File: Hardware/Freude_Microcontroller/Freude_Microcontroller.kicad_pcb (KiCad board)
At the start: 4 copper layers, 20.6 x 22 mm, 22 parts, among them J2 Conn_01x05_Female, J3 Conn_01x06_Female, J4 Conn_01x06_Female, SW1 B3FS-1015P`, U2 STM32L432KBUx, Y1 Crystal_GND24

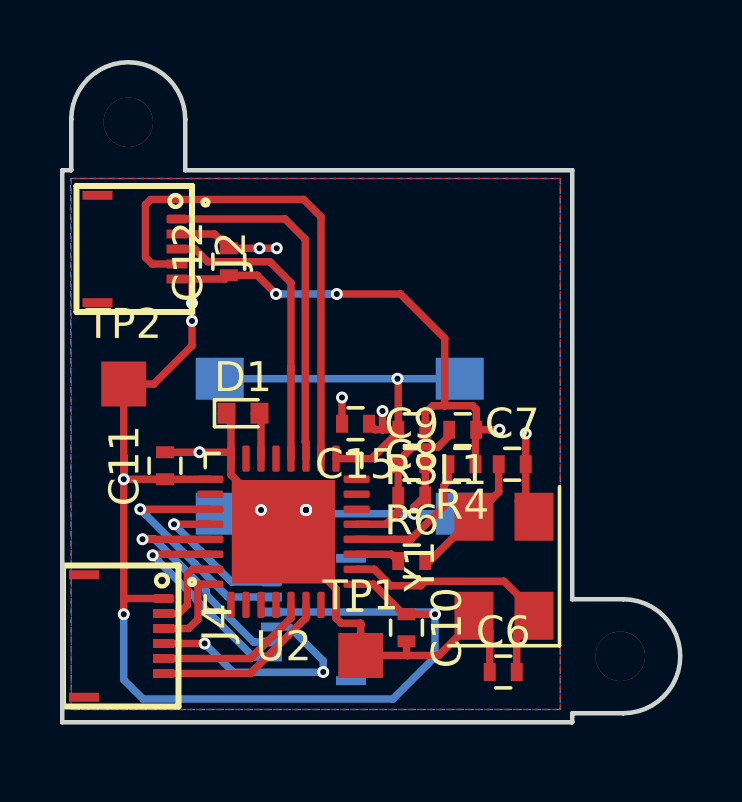
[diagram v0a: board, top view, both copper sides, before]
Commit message: made outline smaller to fit housing, subsequent rerouting
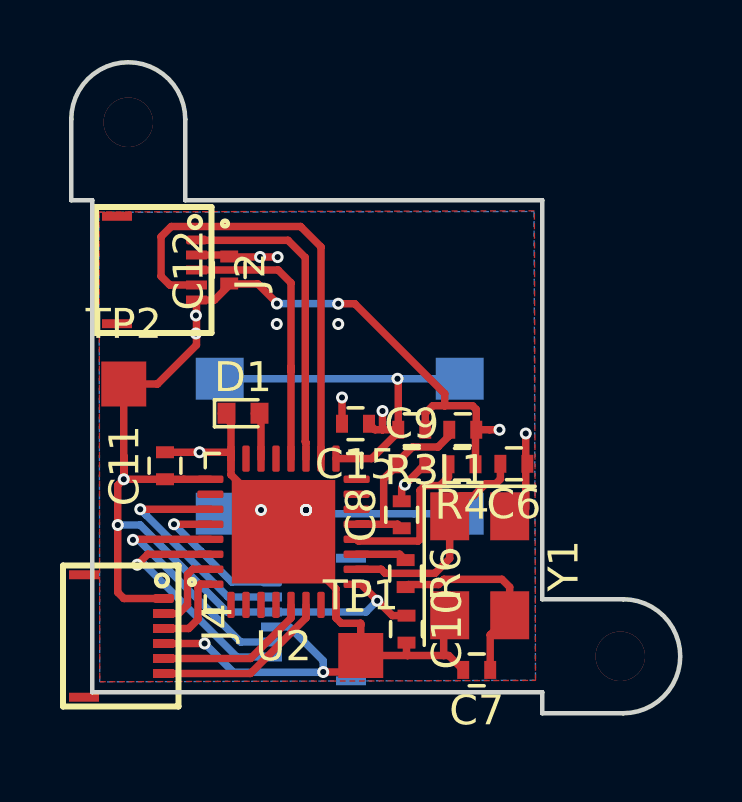
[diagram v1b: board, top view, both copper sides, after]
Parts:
- moved C7 6.96 mm to (205.3, 87.3), turned to 180 degrees
- moved C6 6.95 mm to (206.5, 80.4), turned to 180 degrees
- moved J2 0.96 mm to (195.9, 74.0)
- moved Y1 0.81 mm to (205.4, 83.8), turned to 270 degrees
- moved C8 0.72 mm to (202.8, 82.1), turned to 90 degrees
- moved R6 0.47 mm to (202.9, 84.1), turned to 270 degrees
- moved C12 0.28 mm to (197.0, 74.0)
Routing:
- net +1V8: track 58.4 -> 44.1 mm, vias 8 -> 10
- net GND: track 45.9 -> 44.1 mm
- net /DAC1_OUT2: track 17.1 -> 15.4 mm
- net Net-(C7-Pad1): track 5.14 -> 6.71 mm
- net /DAC2_OUT1: track 11.9 -> 10.5 mm
- net Net-(C6-Pad2): track 8.88 -> 7.55 mm
- net Net-(C8-Pad1): track 5.51 -> 6.68 mm
- net /AZO_UNK: track 7.32 -> 8.33 mm
- net /Switch_Out: track 10.3 -> 9.34 mm
- net /RDY_UC: track 8.06 -> 8.62 mm
- net Net-(R4-Pad2): track 4.83 -> 5.35 mm
- added copper zone on In1.Cu, net +1V8
- removed copper zone on In1.Cu, net +3V3
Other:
- board size 20.6 x 22 mm -> 20.3 x 21.7 mm

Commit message: silk layout, proto release candidate
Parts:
- renumbered REF** to Outline

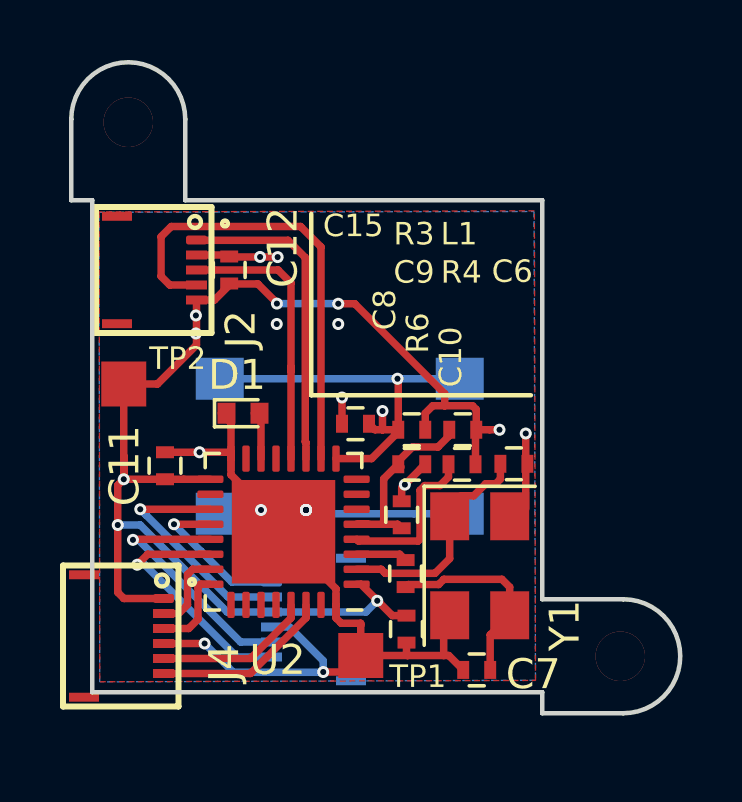
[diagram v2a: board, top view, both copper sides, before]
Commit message: change hole size to 0.45mm, decrease soldermask expansion
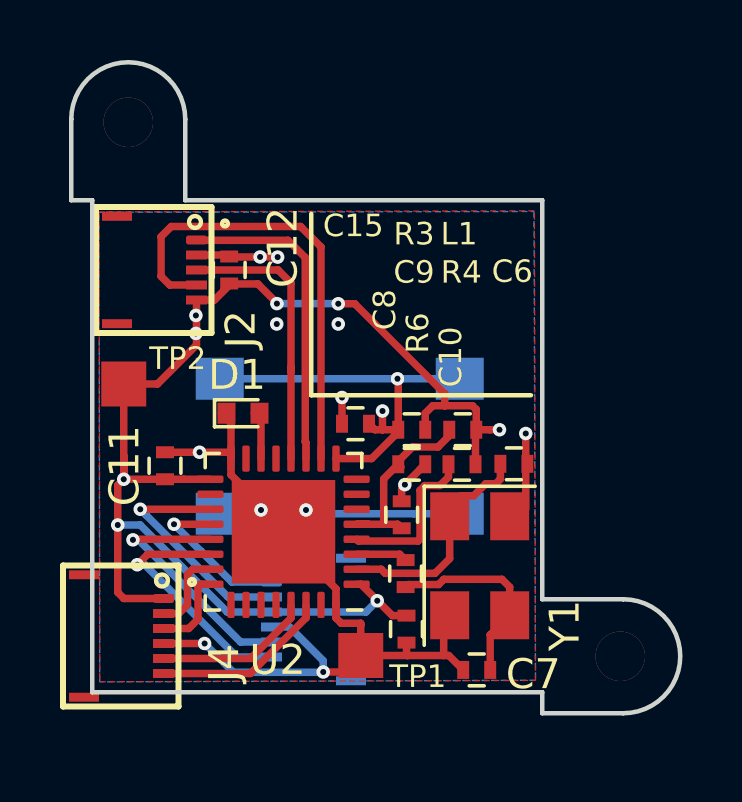
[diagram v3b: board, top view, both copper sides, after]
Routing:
- net GND: vias 14 -> 10

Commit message: resolves #2, resolves #3
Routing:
- net GND: vias 10 -> 13
- net +1V8: vias 10 -> 13
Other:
- rule via_min_size: 0.4 -> 0.45
